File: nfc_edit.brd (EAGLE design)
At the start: 15.4 x 25.1 mm, 5 parts

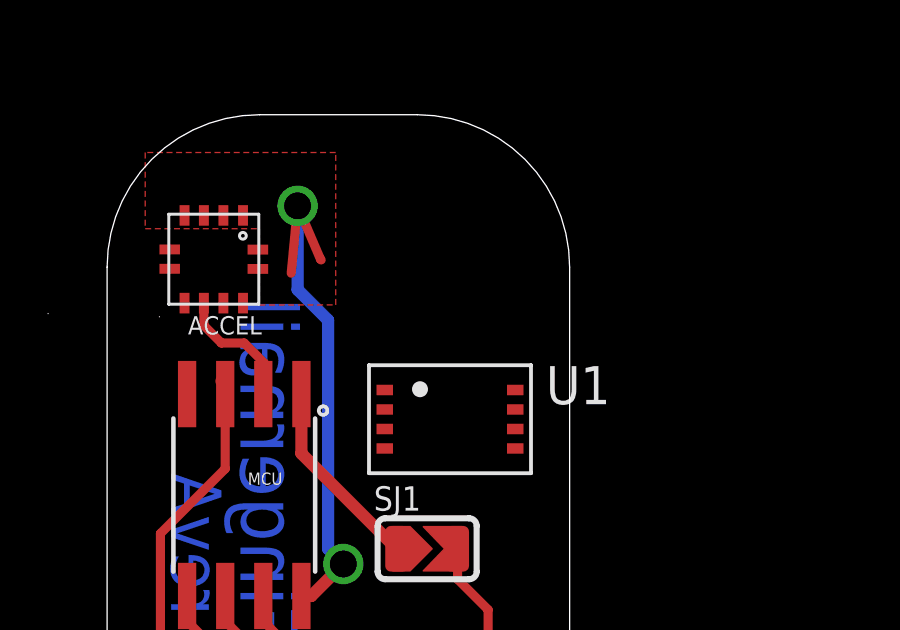
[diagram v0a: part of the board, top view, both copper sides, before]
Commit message: .2uF capacitor has been added
NFC added and connected via power only (no data transfer with ATTiny85)
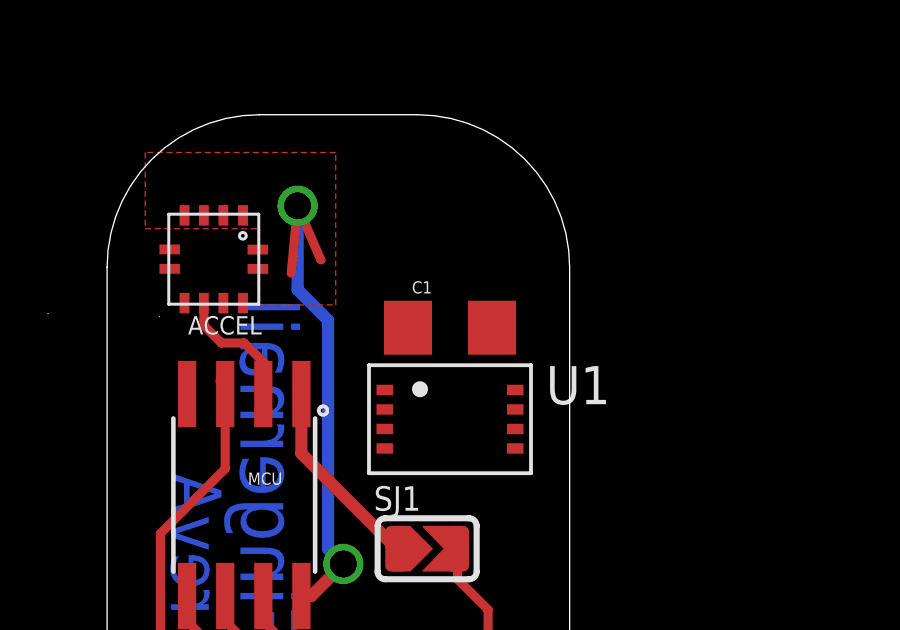
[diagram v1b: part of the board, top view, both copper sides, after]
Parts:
- added C1: 0.2uf, SparkFun-Capacitors:1206
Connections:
- net 2.8V: now also C1.1
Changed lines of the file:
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@@
 <setting verticaltext="up"/>
 </settings>
-<grid distance="0.05" unitdist="inch" unit="inch" style="lines" multiple="1" display="no" altdistance="0.01" altunitdist="inch" altunit="inch"/>
+<grid distance="0.01" unitdist="inch" unit="inch" style="lines" multiple="1" display="no" altdistance="0.01" altunitdist="inch" altunit="inch"/>
 <layers>
 <layer number="1" name="Top" color="4" fill="1" visible="yes" active="yes"/>
@@
 </element>
 <element name="U1" library="AlterNail" package="NT3H1101" value="" x="13.97" y="15.24"/>
+<element name="C1" library="SparkFun-Capacitors" package="1206" value="0.2uf" x="13.97" y="18.288"/>
 </elements>
 <signals>
@@
 <wire x1="9.906" y1="10.922" x2="10.414" y2="10.414" width="0.4064" layer="16"/>
 <contactref element="U1" pad="7"/>
-<wire x1="8.89" y1="22.352" x2="6.416" y2="22.034" width="0" layer="19" extent="1-1"/>
+<contactref element="C1" pad="1"/>
+<wire x1="9.906" y1="18.542" x2="16.145" y2="15.565" width="0" layer="19" extent="1-16"/>
+<wire x1="6.416" y1="22.034" x2="8.89" y2="22.352" width="0" layer="19" extent="1-1"/>
 <wire x1="5.121" y1="19.109" x2="6.416" y2="22.034" width="0" layer="19" extent="1-1"/>
-<wire x1="16.145" y1="15.565" x2="9.017" y2="9.3472" width="0" layer="19" extent="1-1"/>
+<wire x1="12.57" y1="18.288" x2="9.017" y2="9.3472" width="0" layer="19" extent="1-1"/>
 </signal>
 <signal name="VSS/GND">
